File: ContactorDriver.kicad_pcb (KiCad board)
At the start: 2 copper layers, 37 x 66 mm, 32 parts, among them J1 PowerConn, Q1 CSD18511KTT, Q2 CSD18511KTT, Q3 CSD18511KTT, U1 RI3-1212S

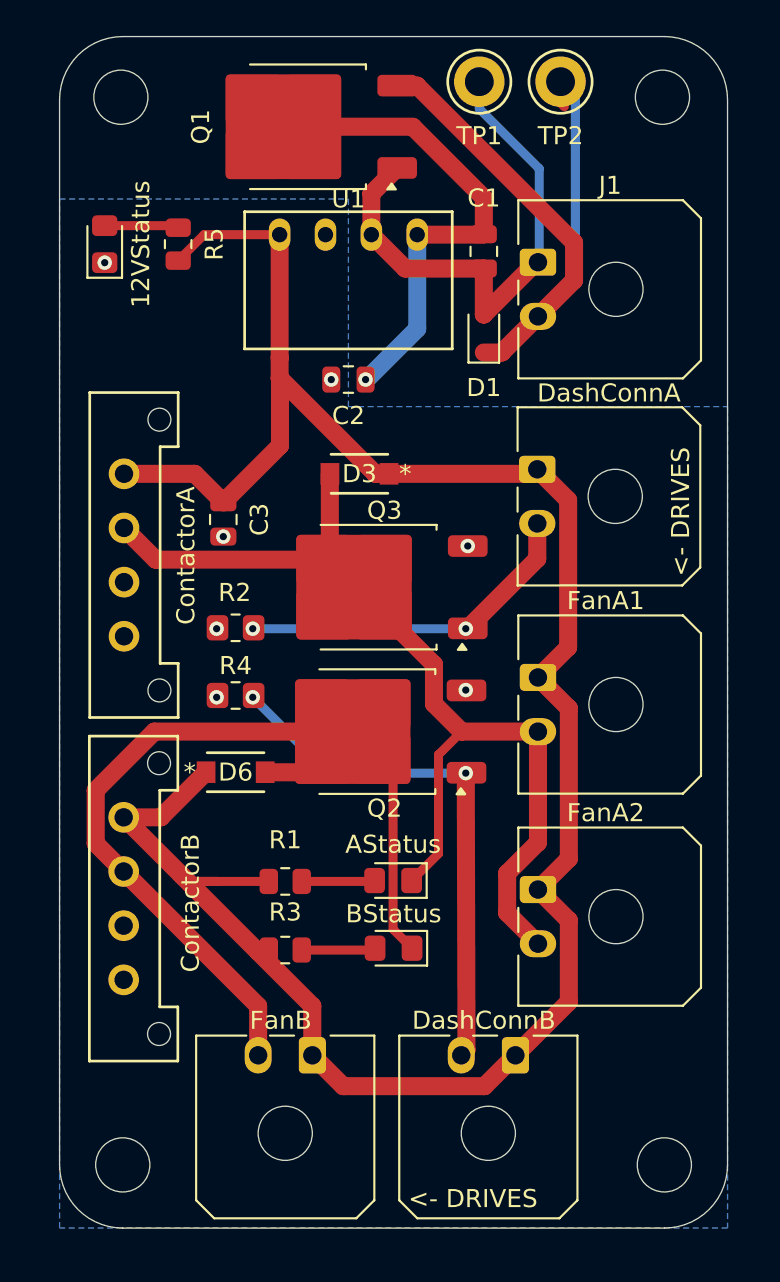
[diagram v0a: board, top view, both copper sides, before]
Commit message: Added images
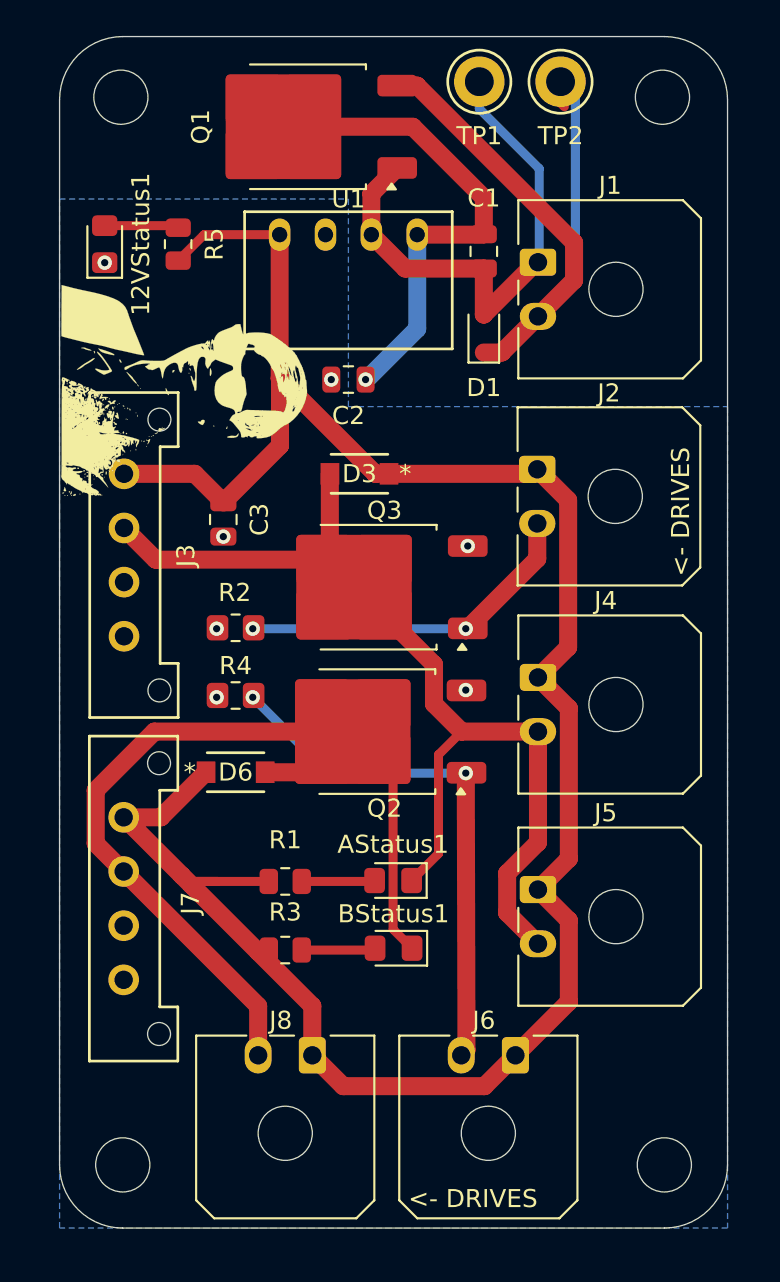
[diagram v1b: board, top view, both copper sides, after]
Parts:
- added LOGO1: Hallock, UTSVT_Special:Hallock_Image_Tiny, F.Cu at (103.7, 65.8)
- added LOGO2: Plusle, Board:plusle, B.Cu at (113.2, 70.9)
- added LOGO3: Minun, Board:minun, B.Cu at (112.9, 90.8)
- renumbered 12VStatus to 12VStatus1, AStatus to AStatus1, BStatus to BStatus1, DashConnA to J2, ContactorA to J3, FanA1 to J4, FanA2 to J5, DashConnB to J6, ContactorB to J7, FanB to J8

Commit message: Updated with vertical conns, new mosfet, and no more isolator
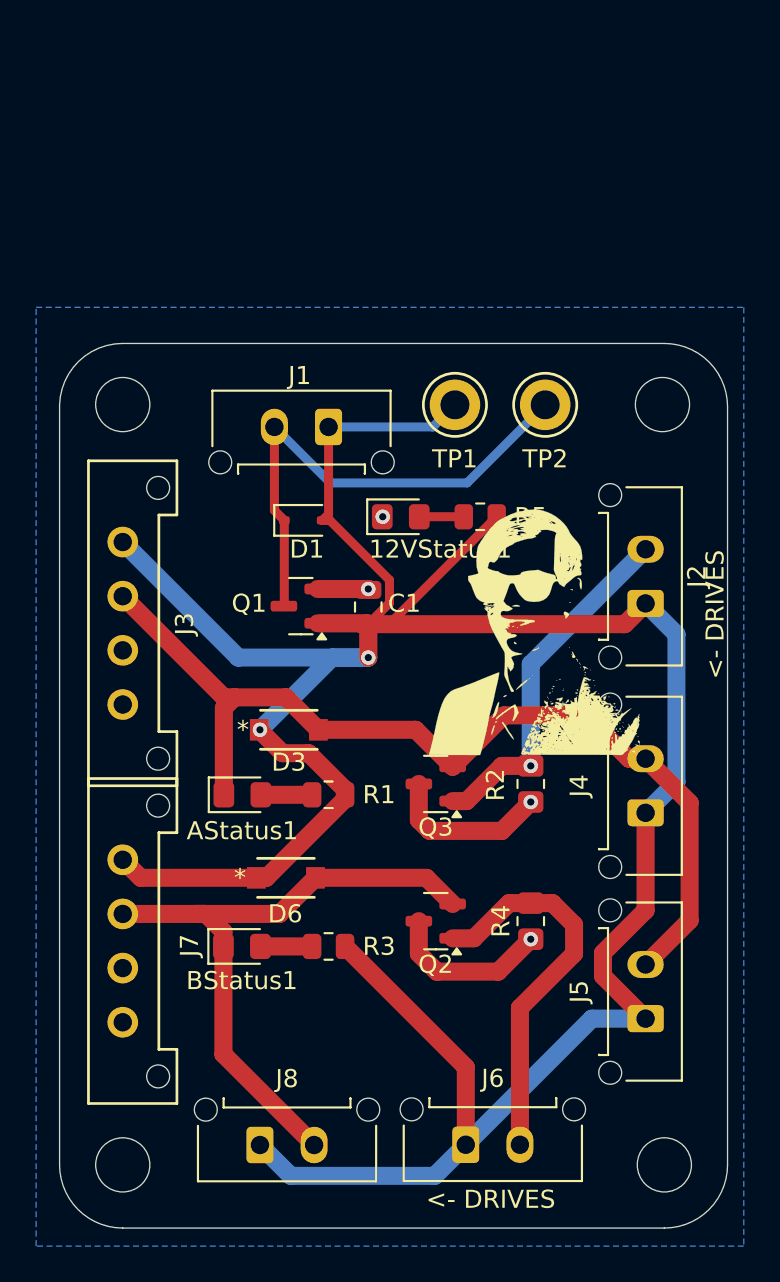
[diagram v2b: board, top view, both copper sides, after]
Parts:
- removed C2: 2.2n, Capacitor_SMD:C_0805_2012Metric
- removed C3: 10u, Capacitor_SMD:C_0805_2012Metric
- removed U1: RI3-1212S, UTSVT_ICs:RI3_DC_Converter
- J1, J2, J4, J5, J6, J8: footprint Connector_Molex:Molex_Micro-Fit_3.0_43650-0200_1x02_P3.00mm_Horizontal -> Connector_Molex:Molex_Micro-Fit_3.0_43650-0215_1x02_P3.00mm_Vertical
- Q1, Q2, Q3: value CSD18511KTT -> IRLML0030TRPbF; footprint Package_TO_SOT_SMD:TO-252-2 -> Package_TO_SOT_SMD:SOT-23
- moved Q1 26.6 mm to (110.0, 78.2)
- moved LOGO2 25.7 mm to (115.7, 96.4), turned to -90 degrees
- moved LOGO1 23.2 mm to (122.4, 79.5), turned to 0 degrees
- moved R5 22.5 mm to (119.9, 73.2), turned to 0 degrees
- moved 12VStatus1 22.3 mm to (115.5, 73.2), turned to 0 degrees
- moved C1 20.7 mm to (113.7, 78.2)
- moved R4 20.6 mm to (122.7, 95.6), turned to 90 degrees
- moved R2 18.5 mm to (122.7, 88.0), turned to 90 degrees
- moved TP1 18.0 mm to (118.5, 67.0)
- moved TP2 17.9 mm to (123.5, 67.0)
- moved H2 17.0 mm to (100.1, 67.0)
- moved H1 17.0 mm to (130.0, 67.0)
- moved J1 14.8 mm to (111.5, 68.3), turned to 180 degrees
- moved D3 14.7 mm to (109.3, 85.0), turned to 0 degrees
- moved D1 14.4 mm to (110.1, 73.4), turned to 0 degrees
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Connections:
- C1 pad 1: Net-(D1-A2) -> +12V
- C1 pad 2: Net-(Q1-D) -> GND
- D1 pad 2: Net-(D1-A2) -> +12V
- J1 pad 1: Net-(D1-A2) -> +12V
- Q1 pad 1: Net-(D1-A2) -> +12V
- Q1 pad 2: Net-(Q1-D) -> GND
- TP1 pad 1: Net-(D1-A2) -> +12V
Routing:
- net +12V: track 126.8 -> 161.9 mm, vias 0 -> 2
- net Net-(D1-A2): track 29.5 -> 0.00 mm
- net Net-(Q1-D): track 27.7 -> 0.00 mm, vias 1 -> 0
- net GND: track 0.00 -> 21.1 mm, vias 7 -> 4
- net /CONTACTOR_B_V-: track 48.6 -> 35.6 mm
- net Net-(D1-A1): track 37.8 -> 28.2 mm
- net Net-(J6-Pin_2): track 29.3 -> 21.5 mm, vias 2 -> 0
- net Net-(12VStatus1-A): track 4.28 -> 2.46 mm
- net Net-(BStatus1-A): track 4.25 -> 2.86 mm
- net Net-(AStatus1-A): track 4.13 -> 2.84 mm
- net Net-(J2-Pin_2): track 19.6 -> 19.8 mm, vias 2 -> 1
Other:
- board size 37 x 66 mm -> 37 x 49 mm

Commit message: Updated to all be 2 pin connectors
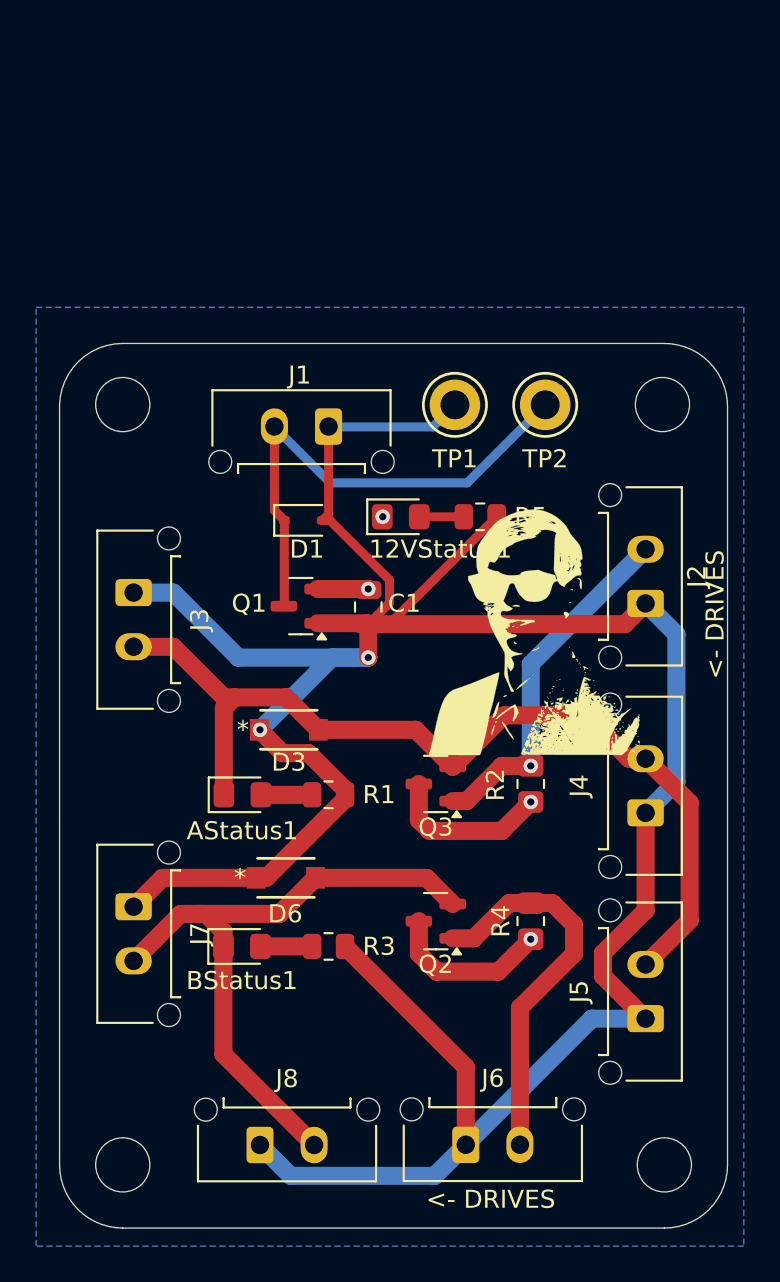
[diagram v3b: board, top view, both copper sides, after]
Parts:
- J3, J7: footprint UTSVT_Connectors:Molex_MicroFit3.0_1x4xP3.00mm_PolarizingPeg_Vertical -> Connector_Molex:Molex_Micro-Fit_3.0_43650-0215_1x02_P3.00mm_Vertical
- moved J3 2.86 mm to (100.7, 77.4)
- moved J7 2.67 mm to (100.7, 94.8)
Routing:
- net +12V: track 161.9 -> 159.7 mm
- net /CONTACTOR_A_V-: track 54.1 -> 52.4 mm

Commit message: Added 12V plane
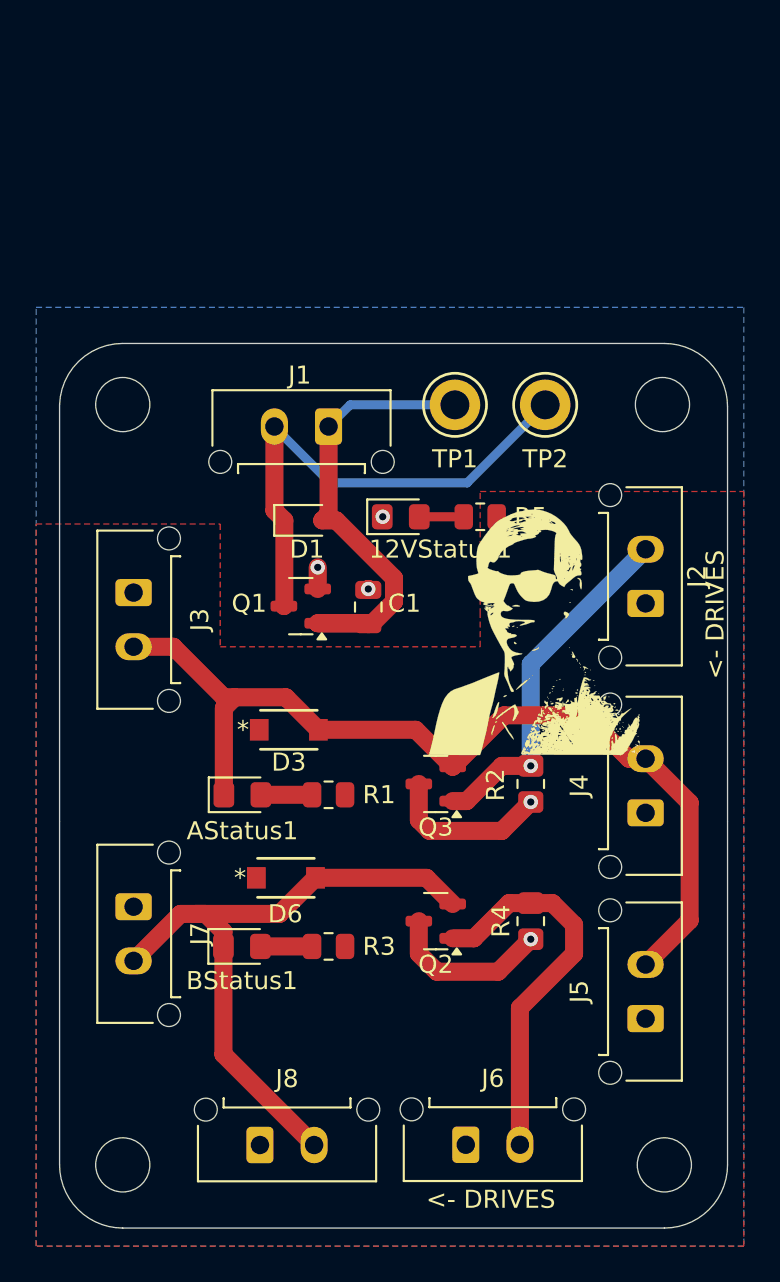
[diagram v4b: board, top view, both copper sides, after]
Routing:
- net +12V: track 159.7 -> 27.0 mm, vias 2 -> 0
- net GND: track 21.1 -> 19.6 mm, vias 4 -> 5
- added copper zone on F.Cu, net +12V

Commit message: Fixed bad planing
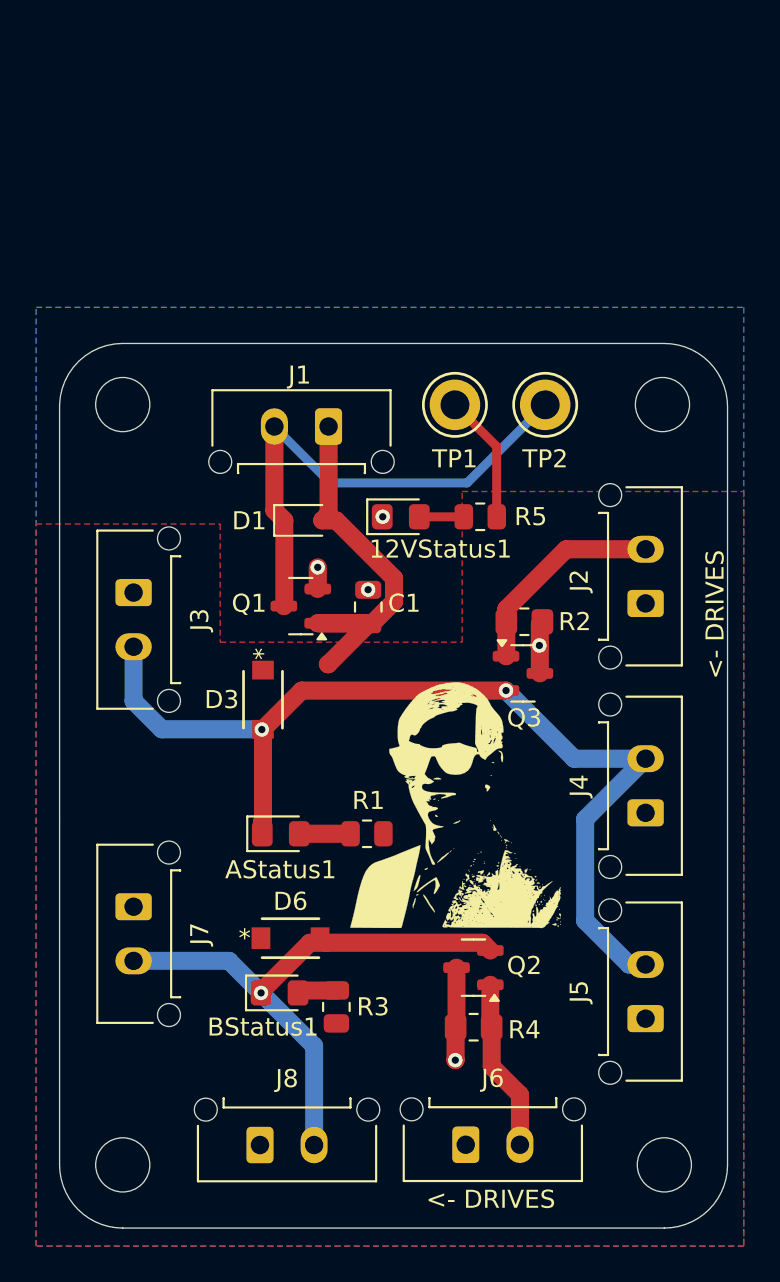
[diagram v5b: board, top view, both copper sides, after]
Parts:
- moved LOGO1 10.5 mm to (118.1, 89.0)
- moved R2 8.99 mm to (122.4, 79.1), turned to 180 degrees
- moved Q3 7.80 mm to (122.3, 81.9), turned to 0 degrees
- moved R4 6.67 mm to (119.5, 101.5), turned to 0 degrees
- moved R3 3.38 mm to (111.9, 100.4), turned to -90 degrees
- moved D6 3.35 mm to (109.4, 96.6)
- moved Q2 3.31 mm to (119.5, 98.2)
- moved BStatus1 3.31 mm to (108.8, 99.6)
- moved R1 3.03 mm to (113.6, 90.8)
- moved AStatus1 3.03 mm to (108.9, 90.8)
- moved D3 2.20 mm to (107.9, 83.4), turned to -90 degrees
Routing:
- net Net-(J6-Pin_2): track 21.5 -> 9.54 mm
- net GND: track 19.6 -> 9.29 mm
- net Net-(J2-Pin_2): track 19.8 -> 11.7 mm, vias 1 -> 0
- net /CONTACTOR_B_V-: track 36.1 -> 31.5 mm, vias 0 -> 1
- net +12V: track 27.0 -> 29.8 mm
- net /CONTACTOR_A_V-: track 52.4 -> 55.0 mm, vias 0 -> 2
- net Net-(BStatus1-A): track 2.86 -> 2.18 mm

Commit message: Reorganized
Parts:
- moved AStatus1 3.62 mm to (108.9, 87.2)
- moved R1 3.62 mm to (113.6, 87.2)
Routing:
- net /CONTACTOR_A_V-: track 55.0 -> 51.5 mm
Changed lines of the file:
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@@
 		(tags "SOT TO_SOT_SMD")
 		(property "Reference" "Q3"
-			(at 0.0785 2.474 360)
+			(at 0.0785 2.474 0)
 			(layer "F.SilkS")
 			(effects
@@
 		)
 		(property "Value" "IRLML0030TRPbF"
-			(at 0 2.4 360)
+			(at 0 2.4 0)
 			(layer "F.Fab")
 			(effects
@@
 		)
 		(fp_text user "${REFERENCE}"
-			(at 0 0 360)
+			(at 0 0 0)
 			(layer "F.Fab")
 			(effects
@@
 	(footprint "Resistor_SMD:R_0805_2012Metric"
 		(layer "F.Cu")
-		(at 113.635 90.8)
+		(at 113.635 87.184)
 		(descr "Resistor SMD 0805 (2012 Metric), square (rectangular) end terminal, IPC_7351 nominal, (Body size source: IPC-SM-782 page 72, https://www.pcb-3d.com/wordpress/wp-content/uploads/ipc-sm-782a_amendment_1_and_2.pdf), generated with kicad-footprint-generator")
 		(tags "resistor")
@@
 		(tags "resistor handsolder")
 		(property "Reference" "R4"
-			(at 2.8093 0.147 360)
+			(at 2.8093 0.147 0)
 			(layer "F.SilkS")
 			(effects
@@
 		)
 		(property "Value" "100k"
-			(at 0 1.65 360)
+			(at 0 1.65 0)
 			(layer "F.Fab")
 			(effects
@@
 		)
 		(fp_text user "${REFERENCE}"
-			(at 0 0 360)
+			(at 0 0 0)
 			(layer "F.Fab")
 			(effects
@@
 		(at 109.397 96.582)
 		(property "Reference" "D6"
-			(at 0 -2.032 360)
+			(at 0 -2.032 0)
 			(layer "F.SilkS")
 			(effects
@@
 		)
 		(property "Value" "V2F22HM3/H"
-			(at 0 0 360)
+			(at 0 0 0)
 			(layer "F.Fab")
 			(effects
@@
 		)
 		(fp_text user "*"
-			(at -2.54 0 360)
+			(at -2.54 0 0)
 			(layer "F.SilkS")
 			(effects
@@
 		)
 		(fp_text user "*"
-			(at -2.54 0 360)
+			(at -2.54 0 0)
 			(layer "F.SilkS")
 			(hide yes)
@@
 		)
 		(fp_text user "0.041in/1.041mm"
-			(at -1.6383 -3.8608 360)
+			(at -1.6383 -3.8608 0)
 			(layer "Dwgs.User")
 			(hide yes)
@@
 		)
 		(fp_text user "0.047in/1.194mm"
-			(at 4.3688 0 360)
+			(at 4.3688 0 0)
 			(layer "Dwgs.User")
 			(hide yes)
@@
 		)
 		(fp_text user "Copyright 2016 Accelerated Designs. All rights reserved."
-			(at 0 0 360)
+			(at 0 0 0)
 			(layer "Cmts.User")
 			(hide yes)
@@
 		)
 		(fp_text user "*"
-			(at -1.1938 0 360)
+			(at -1.1938 0 0)
 			(layer "F.Fab")
 			(hide yes)
@@
 		)
 		(fp_text user "*"
-			(at -1.1938 0 360)
+			(at -1.1938 0 0)
 			(layer "F.Fab")
 			(hide yes)
@@
 	(footprint "LED_SMD:LED_0805_2012Metric_Pad1.15x1.40mm_HandSolder"
 		(layer "F.Cu")
-		(at 108.86 90.8)
+		(at 108.86 87.184)
 		(descr "LED SMD 0805 (2012 Metric), square (rectangular) end terminal, IPC_7351 nominal, (Body size source: https://docs.google.com/spreadsheets/d/1BsfQQcO9C6DZCsRaXUlFlo91Tg2WpOkGARC1WS5S8t0/edit?usp=sharing), generated with kicad-footprint-generator")
 		(tags "LED handsolder")
@@
 	)
 	(segment
-		(start 109.885 90.8)
-		(end 112.7225 90.8)
+		(start 109.885 87.184)
+		(end 112.7225 87.184)
 		(width 1)
 		(layer "F.Cu")
@@
 	)
 	(segment
-		(start 121.335 82.866)
-		(end 110.0193 82.866)
-		(width 1)
-		(layer "F.Cu")
-		(net 6)
-	)
-	(segment
-		(start 110.0193 82.866)
-		(end 107.873 85.0123)
-		(width 1)
-		(layer "F.Cu")
-		(net 6)
-	)
-	(segment
-		(start 107.873 90.062)
-		(end 107.835 90.1)
-		(width 1)
-		(layer "F.Cu")
-		(net 6)
-	)
-	(segment
-		(start 107.835 90.1)
-		(end 107.835 90.8)
+		(start 107.873 85.0123)
+		(end 107.873 87.146)
 		(width 1)
 		(layer "F.Cu")
@@
 	)
 	(segment
-		(start 107.873 85.0123)
-		(end 107.873 90.062)
+		(start 107.873 87.146)
+		(end 107.835 87.184)
 		(width 1)
 		(layer "F.Cu")
@@
 	)
 	(segment
+		(start 109.967309 82.866)
+		(end 121.335 82.866)
+		(width 1)
+		(layer "B.Cu")
+		(net 6)
+	)
+	(segment
 		(start 128.140657 98.04)
 		(end 129.065 98.04)
@@
 		(width 1)
 		(layer "B.Cu")
+		(net 6)
+	)
+	(segment
+		(start 107.807834 85.025475)
+		(end 109.967309 82.866)
+		(width 1)
+		(layer "B.Cu")
